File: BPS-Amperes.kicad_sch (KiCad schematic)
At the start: 34 parts, among them J1 Conn_02x10_Odd_Even, J2 ShuntConn, U1 INA186A3IDDFT, U2 OPA2196, U3 LTC2315, U4 REF1930AIDDCT

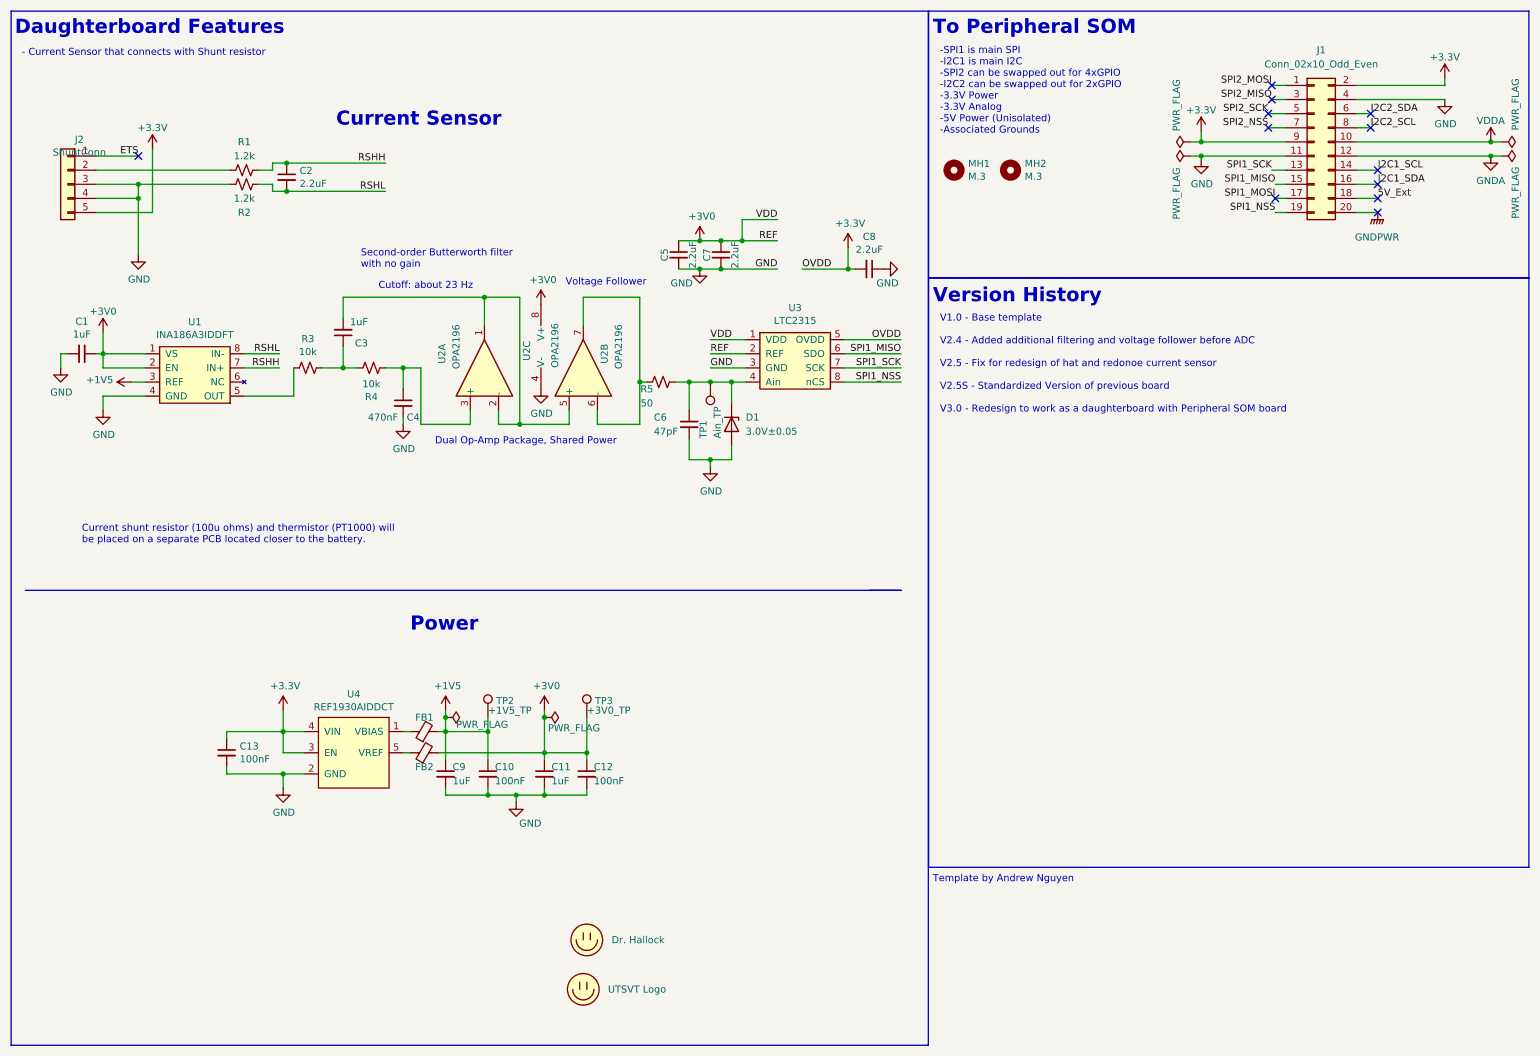
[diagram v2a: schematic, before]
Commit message: Added LED
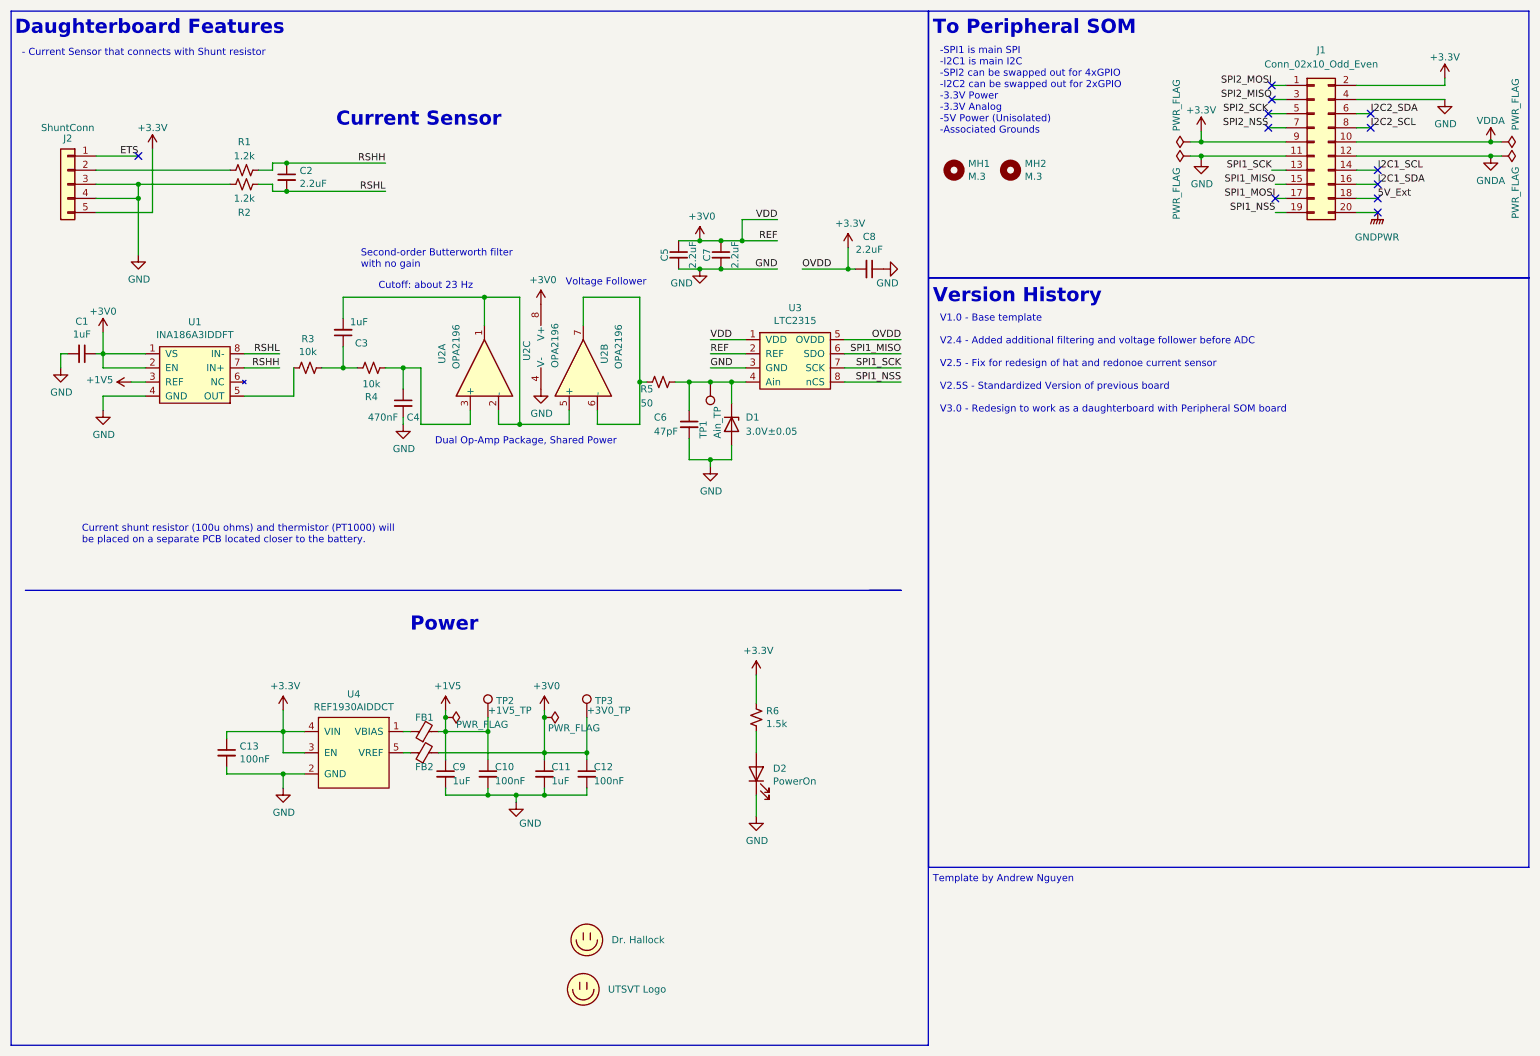
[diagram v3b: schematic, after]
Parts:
- added D2: PowerOn, LED_SMD:LED_0805_2012Metric, symbol Device:LED
- added R6: 1.5k, Resistor_SMD:R_0805_2012Metric, symbol Device:R_Small_US
- renumbered MiniHallock to LOGO0
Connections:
- net +3.3V: now also R6.1
- net GND: now also D2.1 (K)
- new net: D2.2 (A), R6.2
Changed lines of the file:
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@@
+    (stroke (width 0) (type default))
+  )
+  (wire (pts (xy 146.05 153.035) (xy 146.05 156.845))
+    (stroke (width 0) (type default))
+  )
+  (wire (pts (xy 146.05 141.605) (xy 146.05 145.415))
     (stroke (width 0) (type default))
   )
@@
   )
   (wire (pts (xy 107.95 145.415) (xy 107.95 146.685))
+    (stroke (width 0) (type default))
+  )
+  (wire (pts (xy 146.05 131.445) (xy 146.05 136.525))
     (stroke (width 0) (type default))
   )
@@
         (path "/e63e39d7-6ac0-4ffd-8aa3-1841a4541b55"
           (reference "#PWR028") (unit 1)
+        )
+      )
+    )
+  )
+  (symbol (lib_id "power:GND") (at 146.05 156.845 0) (unit 1)
+    (in_bom yes) (on_board yes) (dnp no)
+    (property "Reference" "#PWR029" (at 146.05 163.195 0)
+      (effects (font (size 1.27 1.27)) hide)
+    )
+    (property "Value" "GND" (at 146.177 161.2392 0)
+      (effects (font (size 1.27 1.27)))
+    )
+    (property "Footprint" "" (at 146.05 156.845 0)
+      (effects (font (size 1.27 1.27)) hide)
+    )
+    (property "Datasheet" "" (at 146.05 156.845 0)
+      (effects (font (size 1.27 1.27)) hide)
+    )
+    (pin "1")
+    (instances
+      (project "BPS-Amperes"
+        (path "/637f68f0-cb9c-412a-8573-5d8e7ef6d8a2"
+          (reference "#PWR029") (unit 1)
+        )
+      )
+      (project "BPS-Amperes"
+        (path "/e63e39d7-6ac0-4ffd-8aa3-1841a4541b55"
+          (reference "#PWR011") (unit 1)
         )
       )
@@
   (symbol (lib_id "Connector_Generic:Conn_01x05") (at 22.225 43.18 0) (mirror y) (unit 1)
     (in_bom yes) (on_board yes) (dnp no)
-    (property "Reference" "J2" (at 24.3078 35.1282 0)
-      (effects (font (size 1.27 1.27)))
-    )
-    (property "Value" "ShuntConn" (at 24.3078 37.4396 0)
+    (property "Reference" "J2" (at 22.225 34.925 0)
+      (effects (font (size 1.27 1.27)))
+    )
+    (property "Value" "ShuntConn" (at 22.225 33.02 0)
       (effects (font (size 1.27 1.27)))
     )
@@
     )
   )
+  (symbol (lib_id "power:+3.3V") (at 146.05 131.445 0) (unit 1)
+    (in_bom yes) (on_board yes) (dnp no)
+    (property "Reference" "#PWR028" (at 146.05 135.255 0)
+      (effects (font (size 1.27 1.27)) hide)
+    )
+    (property "Value" "+3.3V" (at 146.431 127.0508 0)
+      (effects (font (size 1.27 1.27)))
+    )
+    (property "Footprint" "" (at 146.05 131.445 0)
+      (effects (font (size 1.27 1.27)) hide)
+    )
+    (property "Datasheet" "" (at 146.05 131.445 0)
+      (effects (font (size 1.27 1.27)) hide)
+    )
+    (pin "1")
+    (instances
+      (project "BPS-Amperes"
+        (path "/637f68f0-cb9c-412a-8573-5d8e7ef6d8a2"
+          (reference "#PWR028") (unit 1)
+        )
+      )
+      (project "BPS-Amperes"
+        (path "/e63e39d7-6ac0-4ffd-8aa3-1841a4541b55"
+          (reference "#PWR010") (unit 1)
+        )
+      )
+    )
+  )
   (symbol (lib_id "Connector:TestPoint") (at 115.57 139.065 0) (unit 1)
     (in_bom yes) (on_board yes) (dnp no)
@@
   (symbol (lib_id "utsvt-misc:Logo_Placeholder") (at 115.57 179.07 0) (unit 1)
     (in_bom yes) (on_board yes) (dnp no) (fields_autoplaced)
-    (property "Reference" "MiniHallock" (at 115.57 175.26 0)
+    (property "Reference" "LOGO0" (at 115.57 175.26 0)
       (effects (font (size 1.27 1.27)) hide)
     )
@@
       (project "BPS-Amperes"
         (path "/637f68f0-cb9c-412a-8573-5d8e7ef6d8a2"
-          (reference "MiniHallock") (unit 1)
+          (reference "LOGO0") (unit 1)
         )
       )
@@
         )
       )
+    )
+  )
+  (symbol (lib_id "Device:R_Small_US") (at 146.05 139.065 0) (unit 1)
+    (in_bom yes) (on_board yes) (dnp no)
+    (property "Reference" "R6" (at 147.828 137.8966 0)
+      (effects (font (size 1.27 1.27)) (justify left))
+    )
+    (property "Value" "1.5k" (at 147.828 140.208 0)
+      (effects (font (size 1.27 1.27)) (justify left))
+    )
+    (property "Footprint" "Resistor_SMD:R_0805_2012Metric" (at 146.05 139.065 0)
+      (effects (font (size 1.27 1.27)) hide)
+    )
+    (property "Datasheet" "~" (at 146.05 139.065 0)
+      (effects (font (size 1.27 1.27)) hide)
+    )
+    (property "Mfg" "CRCW08051K50JNEB" (at 146.05 139.065 0)
+      (effects (font (size 1.27 1.27)) hide)
+    )
+    (pin "1")
+    (pin "2")
+    (instances
+      (project "BPS-Amperes"
+        (path "/637f68f0-cb9c-412a-8573-5d8e7ef6d8a2"
+          (reference "R6") (unit 1)
+        )
+      )
+      (project "BPS-Amperes"
+        (path "/e63e39d7-6ac0-4ffd-8aa3-1841a4541b55"
+          (reference "R2") (unit 1)
+        )
+      )
+    )
+  )
+  (symbol (lib_id "Device:LED") (at 146.05 149.225 90) (unit 1)
+    (in_bom yes) (on_board yes) (dnp no)
+    (property "Reference" "D2" (at 149.0472 148.2344 90)
+      (effects (font (size 1.27 1.27)) (justify right))
+    )
+    (property "Value" "PowerOn" (at 149.0472 150.5458 90)
+      (effects (font (size 1.27 1.27)) (justify right))
+    )
+    (property "Footprint" "LED_SMD:LED_0805_2012Metric" (at 146.05 149.225 0)
+      (effects (font (size 1.27 1.27)) hide)
+    )
+    (property "Datasheet" "~" (at 146.05 149.225 0)
+      (effects (font (size 1.27 1.27)) hide)
+    )
+    (property "Mfg" "APTD2012LCGCK" (at 146.05 149.225 90)
+      (effects (font (size 1.27 1.27)) hide)
+    )
+    (pin "1")
+    (pin "2")
+    (instances
+      (project "BPS-Amperes"
+        (path "/637f68f0-cb9c-412a-8573-5d8e7ef6d8a2"
+          (reference "D2") (unit 1)
+        )
+      )
+      (project "BPS-Amperes"
+        (path "/e63e39d7-6ac0-4ffd-8aa3-1841a4541b55"
+          (reference "D1") (unit 1)
+        )
+      )

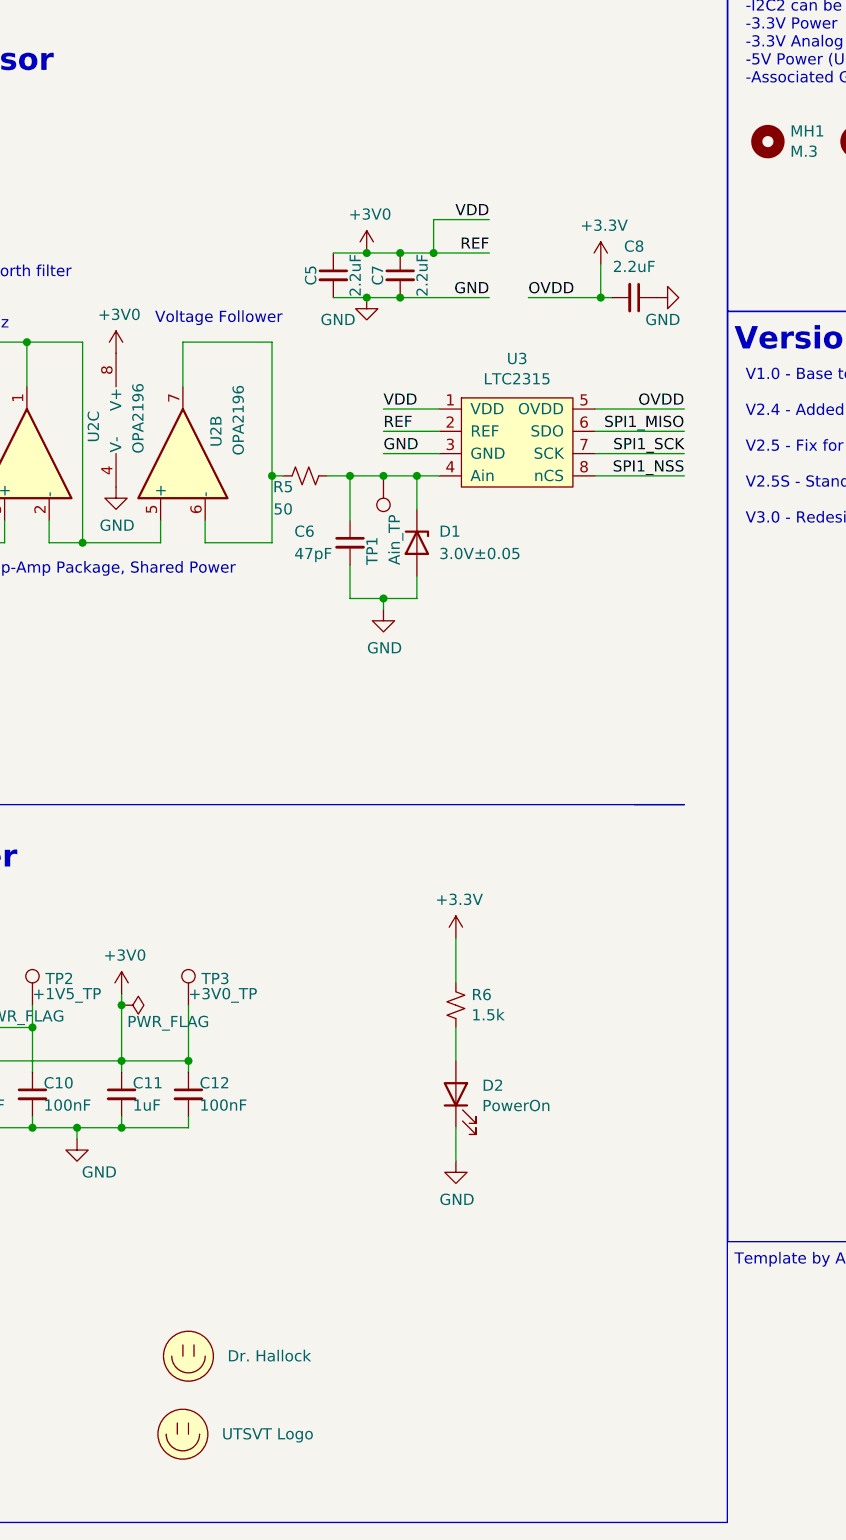
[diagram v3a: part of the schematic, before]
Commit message: Added BOM files
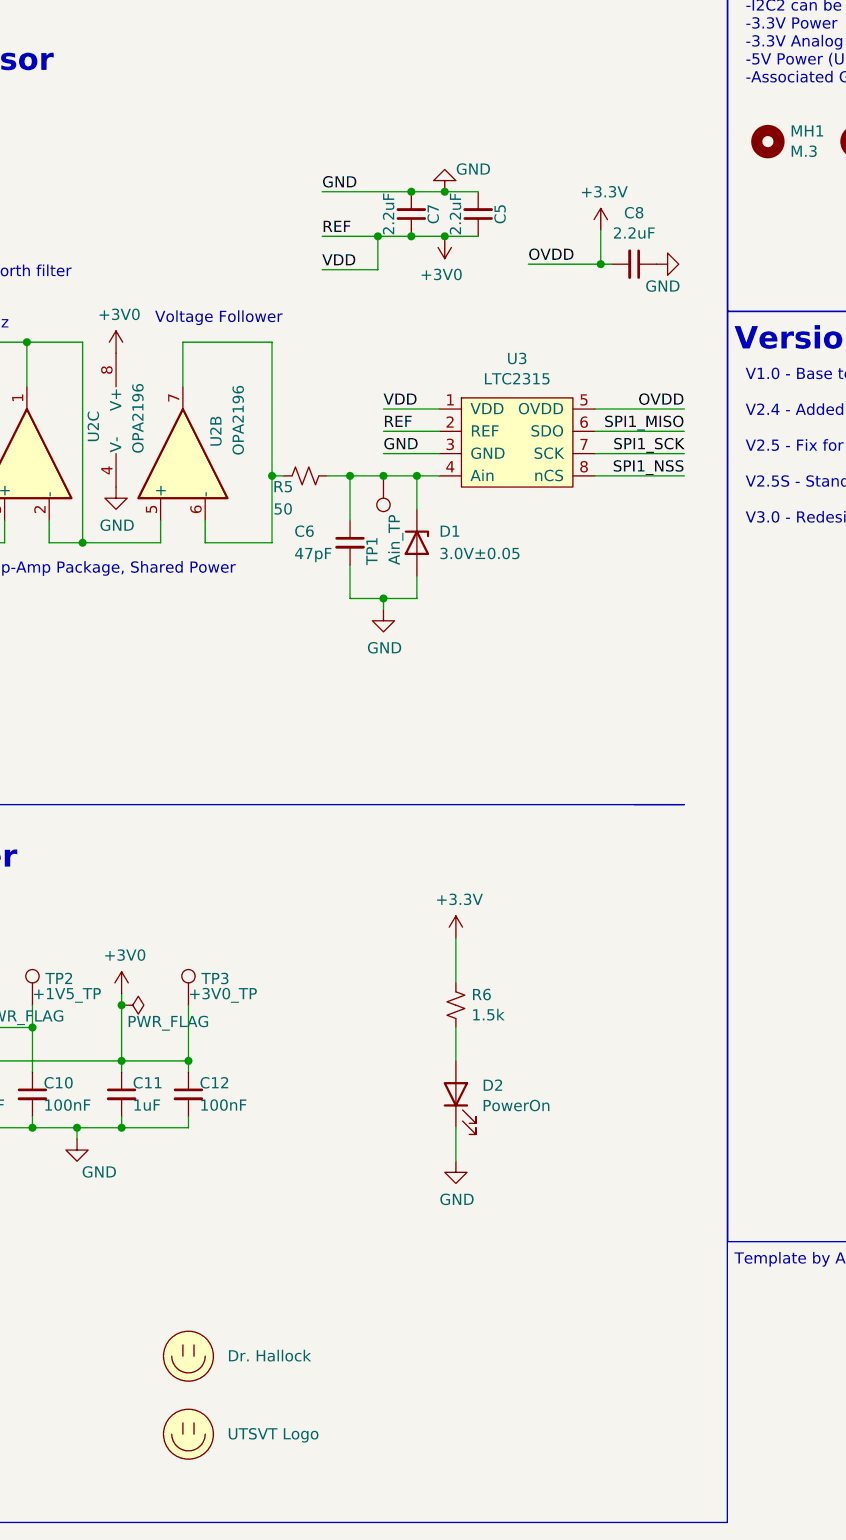
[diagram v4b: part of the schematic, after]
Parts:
- U3: Mfg 584-C2315ITS8-12TMPF -> LTC2315ITS8-12#TRMPBF
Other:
- moved on the sheet: C5, C7, C8
